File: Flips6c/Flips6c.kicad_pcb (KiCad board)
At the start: 2 copper layers, 90 x 50 mm, 20 parts, among them CN1 Conn_02x04_Odd_Even, U1 74HCT595, U2 74HCT595, U3 74HCT595

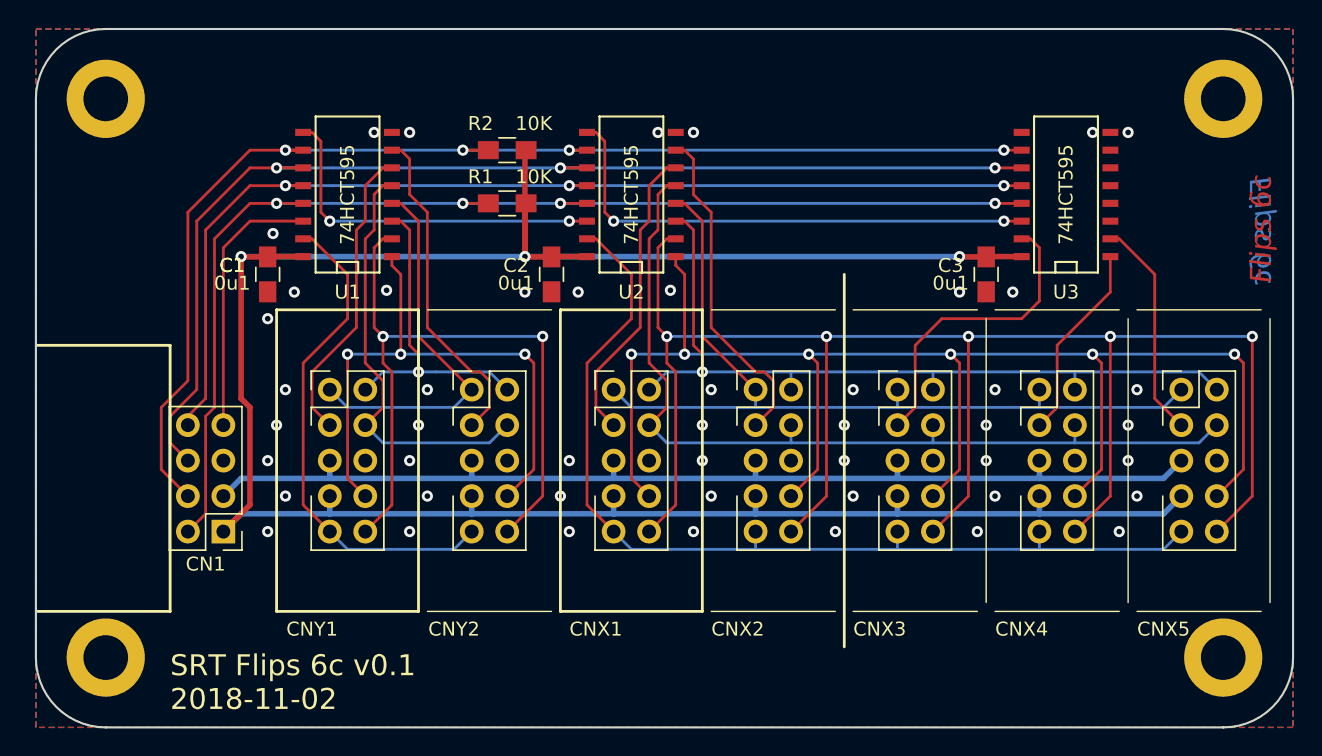
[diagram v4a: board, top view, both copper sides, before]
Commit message: improve 595 5v supply tracing
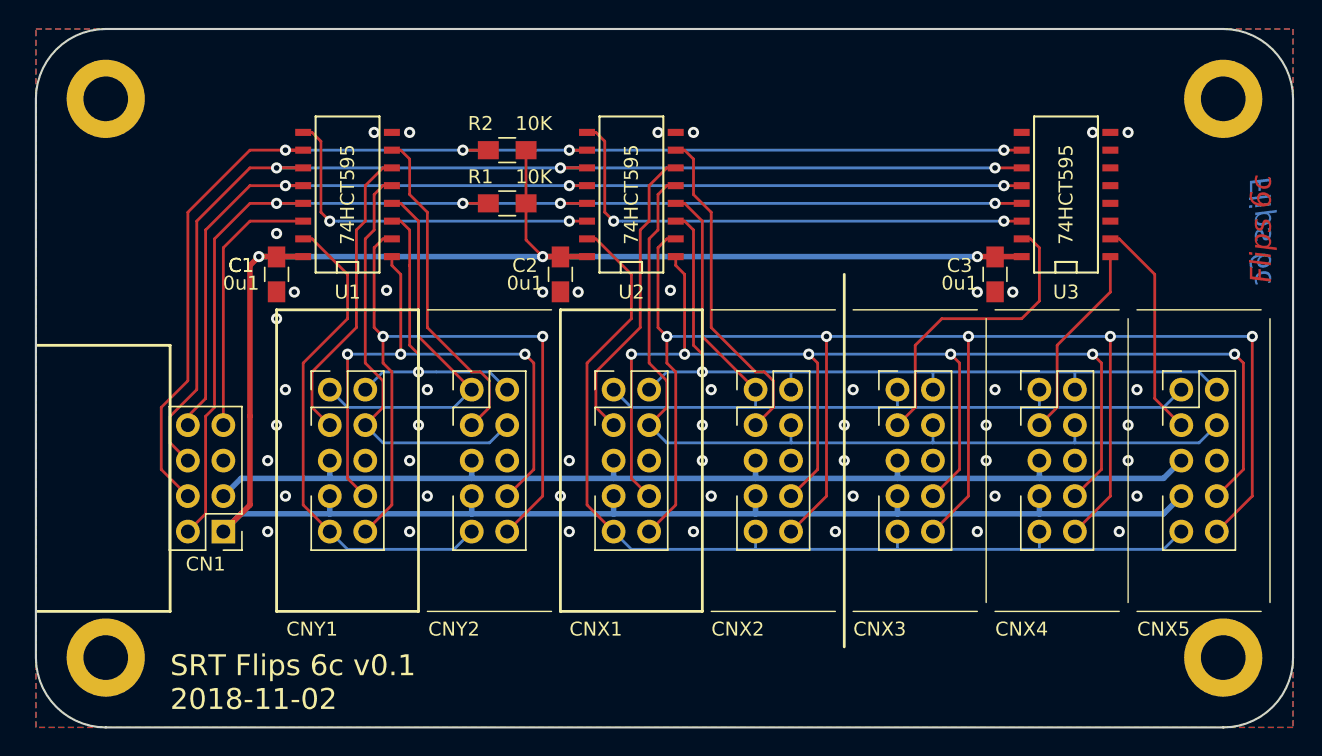
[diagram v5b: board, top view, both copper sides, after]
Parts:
- moved C2 0.64 mm to (209.6, 75.6)
- moved C1 0.63 mm to (189.2, 75.6)
- moved C3 0.63 mm to (240.7, 75.6)
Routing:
- net +5V: track 174.3 -> 167.2 mm
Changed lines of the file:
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@@
   )
   (module Capacitors_SMD:C_0805_HandSoldering (layer F.Cu)
-    (at 188.595 75.565 270)
+    (at 189.23 75.565 270)
     (descr "Capacitor SMD 0805, hand soldering")
     (tags "capacitor 0805")
@@
   )
   (module Capacitors_SMD:C_0805_HandSoldering (layer F.Cu)
-    (at 208.915 75.565 270)
+    (at 209.55 75.565 270)
     (descr "Capacitor SMD 0805, hand soldering")
     (tags "capacitor 0805")
@@
   )
   (module Capacitors_SMD:C_0805_HandSoldering (layer F.Cu)
-    (at 240.03 75.565 270)
+    (at 240.665 75.565 270)
     (descr "Capacitor SMD 0805, hand soldering")
     (tags "capacitor 0805")
@@
   (segment (start 233.68 91.44) (end 233.68 92.71) (width 0.4) (layer B.Cu) (net 1) (status 400010))
   (segment (start 243.84 91.44) (end 243.84 92.71) (width 0.4) (layer B.Cu) (net 1) (status 400010))
-  (segment (start 191.135 74.295) (end 188.595 74.295) (width 0.4) (layer F.Cu) (net 1) (status C00030))
-  (segment (start 211.455 74.295) (end 208.875 74.295) (width 0.4) (layer F.Cu) (net 1) (status C00030))
-  (segment (start 240.01 74.295) (end 242.57 74.295) (width 0.4) (layer F.Cu) (net 1) (status C00030))
-  (segment (start 240.03 74.315) (end 238.145 74.315) (width 0.4) (layer F.Cu) (net 1) (status 400010))
-  (segment (start 238.145 74.315) (end 238.125 74.295) (width 0.4) (layer F.Cu) (net 1))
-  (segment (start 207.03 74.315) (end 208.915 74.315) (width 0.4) (layer F.Cu) (net 1) (status 800020))
-  (segment (start 207.01 74.295) (end 207.03 74.315) (width 0.4) (layer F.Cu) (net 1))
-  (via (at 207.01 74.295) (size 0.8) (drill 0.4) (layers F.Cu B.Cu) (net 1))
-  (segment (start 238.125 74.295) (end 207.01 74.295) (width 0.4) (layer B.Cu) (net 1))
-  (via (at 238.125 74.295) (size 0.8) (drill 0.4) (layers F.Cu B.Cu) (net 1))
-  (segment (start 207.01 74.295) (end 186.69 74.295) (width 0.4) (layer B.Cu) (net 1))
-  (segment (start 186.71 74.315) (end 188.595 74.315) (width 0.4) (layer F.Cu) (net 1) (status 800020))
-  (segment (start 186.69 74.295) (end 186.71 74.315) (width 0.4) (layer F.Cu) (net 1))
-  (via (at 186.69 74.295) (size 0.8) (drill 0.4) (layers F.Cu B.Cu) (net 1))
-  (segment (start 186.69 74.295) (end 186.69 84.455) (width 0.4) (layer F.Cu) (net 1))
+  (segment (start 211.455 74.295) (end 209.51 74.295) (width 0.4) (layer F.Cu) (net 1) (status C00020))
+  (segment (start 240.645 74.295) (end 242.57 74.295) (width 0.4) (layer F.Cu) (net 1) (status C00010))
+  (via (at 239.395 74.295) (size 0.8) (drill 0.4) (layers F.Cu B.Cu) (net 1))
+  (segment (start 239.395 74.295) (end 208.28 74.295) (width 0.4) (layer B.Cu) (net 1))
+  (via (at 208.28 74.295) (size 0.8) (drill 0.4) (layers F.Cu B.Cu) (net 1))
+  (segment (start 187.325 85.725) (end 187.325 92.075) (width 0.4) (layer F.Cu) (net 1))
   (segment (start 187.325 92.075) (end 185.42 93.98) (width 0.4) (layer F.Cu) (net 1) (status 800020))
-  (segment (start 187.325 85.09) (end 187.325 92.075) (width 0.4) (layer F.Cu) (net 1))
-  (segment (start 186.69 84.455) (end 187.325 85.09) (width 0.4) (layer F.Cu) (net 1))
-  (segment (start 207.09 70.485) (end 207.01 70.565) (width 0.4) (layer F.Cu) (net 1) (status C00030))
-  (segment (start 207.01 70.565) (end 207.01 74.295) (width 0.4) (layer F.Cu) (net 1) (status 400010))
-  (segment (start 207.01 74.295) (end 207.01 66.755) (width 0.4) (layer F.Cu) (net 1) (status 800020))
-  (segment (start 207.01 66.755) (end 207.09 66.675) (width 0.4) (layer F.Cu) (net 1) (status C00030))
+  (segment (start 191.135 74.295) (end 189.25 74.295) (width 0.4) (layer F.Cu) (net 1) (status C00000))
+  (segment (start 189.25 74.295) (end 189.23 74.315) (width 0.4) (layer F.Cu) (net 1) (status C00000))
+  (segment (start 189.23 74.315) (end 189.21 74.295) (width 0.4) (layer F.Cu) (net 1) (status C00000))
+  (via (at 187.96 74.295) (size 0.8) (drill 0.4) (layers F.Cu B.Cu) (net 1))
+  (segment (start 187.96 74.295) (end 208.28 74.295) (width 0.4) (layer B.Cu) (net 1))
+  (segment (start 189.21 74.295) (end 187.96 74.295) (width 0.4) (layer F.Cu) (net 1) (status 400000))
+  (segment (start 187.96 74.295) (end 187.325 74.93) (width 0.4) (layer F.Cu) (net 1))
+  (segment (start 187.325 85.725) (end 187.325 74.93) (width 0.4) (layer F.Cu) (net 1))
+  (segment (start 208.28 74.295) (end 209.53 74.295) (width 0.4) (layer F.Cu) (net 1))
+  (segment (start 209.53 74.295) (end 209.55 74.315) (width 0.4) (layer F.Cu) (net 1) (status C00000))
+  (segment (start 240.665 74.315) (end 240.645 74.295) (width 0.4) (layer F.Cu) (net 1) (status C00000))
+  (segment (start 240.645 74.295) (end 239.395 74.295) (width 0.4) (layer F.Cu) (net 1) (status 400000))
+  (segment (start 208.28 74.295) (end 207.09 73.105) (width 0.2) (layer F.Cu) (net 1))
+  (segment (start 207.09 73.105) (end 207.09 70.485) (width 0.2) (layer F.Cu) (net 1) (status 800000))
+  (segment (start 207.09 70.485) (end 207.09 66.675) (width 0.2) (layer F.Cu) (net 1) (status C00000))
   (via (at 198.755 93.98) (size 0.8) (drill 0.4) (layers F.Cu B.Cu) (net 2))
   (via (at 200.025 91.44) (size 0.8) (drill 0.4) (layers F.Cu B.Cu) (net 2))
@@
   (via (at 250.19 86.36) (size 0.8) (drill 0.4) (layers F.Cu B.Cu) (net 2))
   (via (at 250.825 83.82) (size 0.8) (drill 0.4) (layers F.Cu B.Cu) (net 2))
-  (via (at 238.125 76.835) (size 0.8) (drill 0.4) (layers F.Cu B.Cu) (net 2))
+  (via (at 239.395 76.835) (size 0.8) (drill 0.4) (layers F.Cu B.Cu) (net 2))
   (via (at 241.935 76.835) (size 0.8) (drill 0.4) (layers F.Cu B.Cu) (net 2))
   (via (at 216.535 65.405) (size 0.8) (drill 0.4) (layers F.Cu B.Cu) (net 2))
@@
   (via (at 198.755 65.405) (size 0.8) (drill 0.4) (layers F.Cu B.Cu) (net 2))
   (via (at 210.82 76.835) (size 0.8) (drill 0.4) (layers F.Cu B.Cu) (net 2))
-  (via (at 207.01 76.835) (size 0.8) (drill 0.4) (layers F.Cu B.Cu) (net 2))
-  (via (at 188.595 78.74) (size 0.8) (drill 0.4) (layers F.Cu B.Cu) (net 2))
+  (via (at 208.28 76.835) (size 0.8) (drill 0.4) (layers F.Cu B.Cu) (net 2))
+  (via (at 189.23 78.74) (size 0.8) (drill 0.4) (layers F.Cu B.Cu) (net 2))
   (via (at 190.5 76.835) (size 0.8) (drill 0.4) (layers F.Cu B.Cu) (net 2))
   (via (at 197.104 76.708) (size 0.8) (drill 0.4) (layers F.Cu B.Cu) (net 2))
@@
   (via (at 247.65 65.405) (size 0.8) (drill 0.4) (layers F.Cu B.Cu) (net 2))
   (via (at 250.19 65.405) (size 0.8) (drill 0.4) (layers F.Cu B.Cu) (net 2))
-  (via (at 188.976 72.644) (size 0.8) (drill 0.4) (layers F.Cu B.Cu) (net 2))
+  (via (at 189.23 72.644) (size 0.8) (drill 0.4) (layers F.Cu B.Cu) (net 2))
   (via (at 188.595 88.9) (size 0.8) (drill 0.4) (layers F.Cu B.Cu) (net 2))
   (via (at 188.595 93.98) (size 0.8) (drill 0.4) (layers F.Cu B.Cu) (net 2))

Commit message: reworking gnd vias
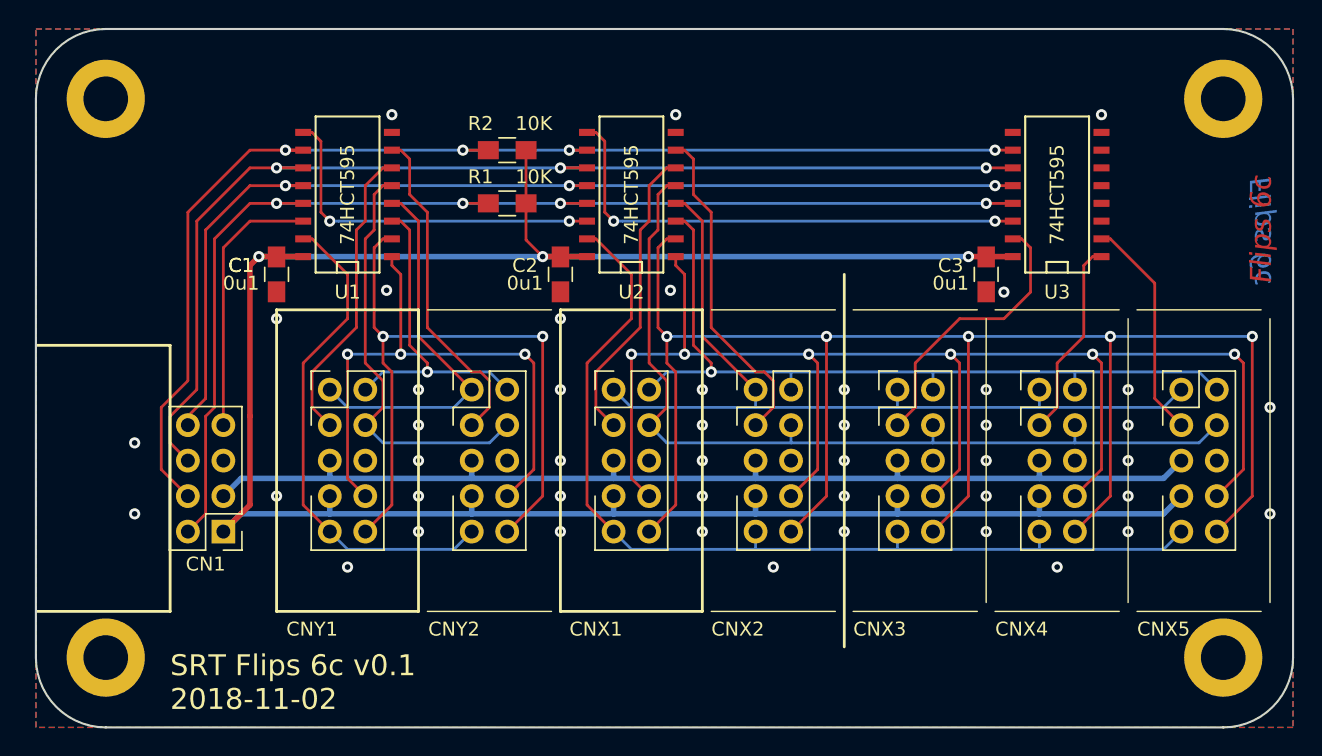
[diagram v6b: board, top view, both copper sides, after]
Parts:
- moved C3 0.63 mm to (240.0, 75.6)
- moved U3 0.63 mm to (245.1, 69.8)
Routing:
- net /XEN3: track 21.8 -> 20.0 mm
- net /~OE: track 86.2 -> 85.6 mm
- net Net-(U2-Pad9): track 36.7 -> 36.1 mm
- net /~SRCLR: track 89.1 -> 88.4 mm
- net /SRCLK: track 82.9 -> 82.3 mm
- net /RCLK: track 78.0 -> 77.4 mm
- net +5V: track 167.2 -> 166.5 mm
- net GND: vias 48 -> 45

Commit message: rework silk screen
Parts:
- added REF**: KiCAD Logo, Symbols:Symbol_KiCAD-Logo_CopperAndSilkScreenTop, F.Cu at (246.4, 104.8)
- added REF***: OSHW-Logo2_7.3x6mm_SilkScreen, Symbols:OSHW-Logo2_7.3x6mm_SilkScreen, F.Cu at (236.2, 104.8)
- added REF***: WEEE-Logo_4.2x6mm_SilkScreen, Symbols:WEEE-Logo_4.2x6mm_SilkScreen, B.Cu at (185.4, 103.5)
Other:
- board text added: "FLIPS"
- board text added: "SRT Flips 6c V1.0 2018-11-02 github.com/cawapy/FlipSuite"
- board text added: "back"
- board text added: "front"
- board text removed: "Flips 6c"
- board text removed: "SRT"
- board text removed: "SRT Flips 6c v0.1 2018-11-02"
